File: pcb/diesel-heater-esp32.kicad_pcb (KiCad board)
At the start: 2 copper layers, 60 x 45 mm, 29 parts, among them J1 5V Power, J10 Fan Motor, J11 Glow Plug, J12 Oil Pump, J2 ESP32 Left, J3 Hall Sensor, J4 Buttons, J5 Battery Mon, J6 ESP32 Right, J7 OLED, J8 NTC50K Room Temperatire, J9 NTC50K Outlet Temperatire

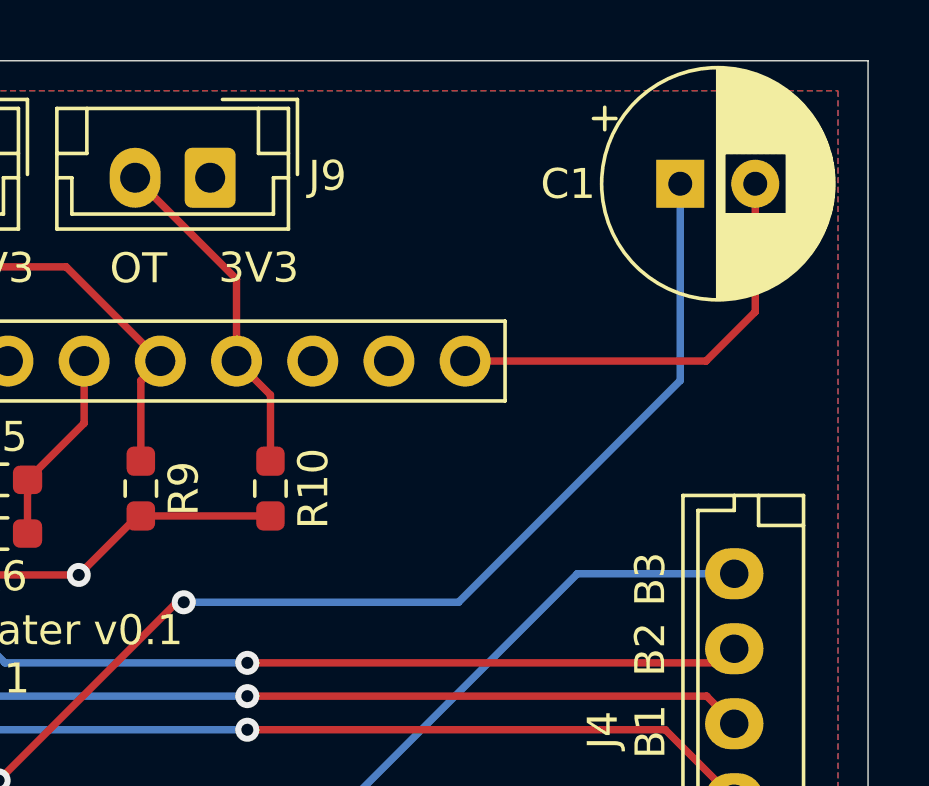
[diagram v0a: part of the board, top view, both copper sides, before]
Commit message: capacitor value fixed. capacitor sized set to 6.3mm
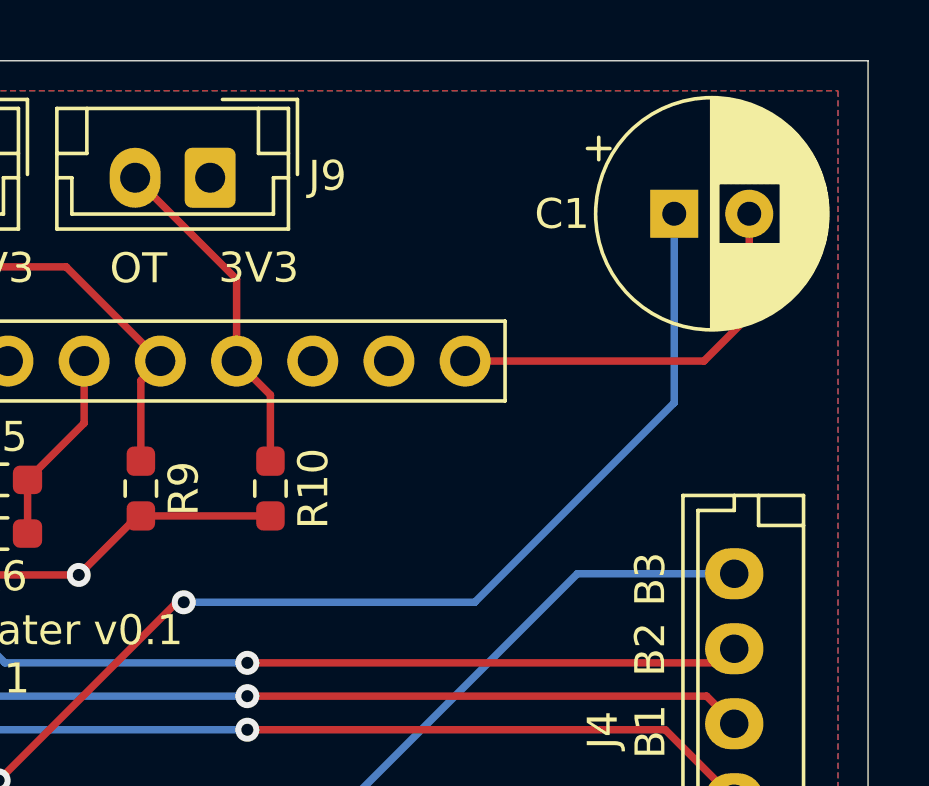
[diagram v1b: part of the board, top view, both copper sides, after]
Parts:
- C1: value CP1 -> 470uF
- moved C1 1.02 mm to (167.8, 73.0)
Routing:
- net /EN: track 14.6 -> 13.5 mm
- net /5V: track 73.1 -> 72.3 mm

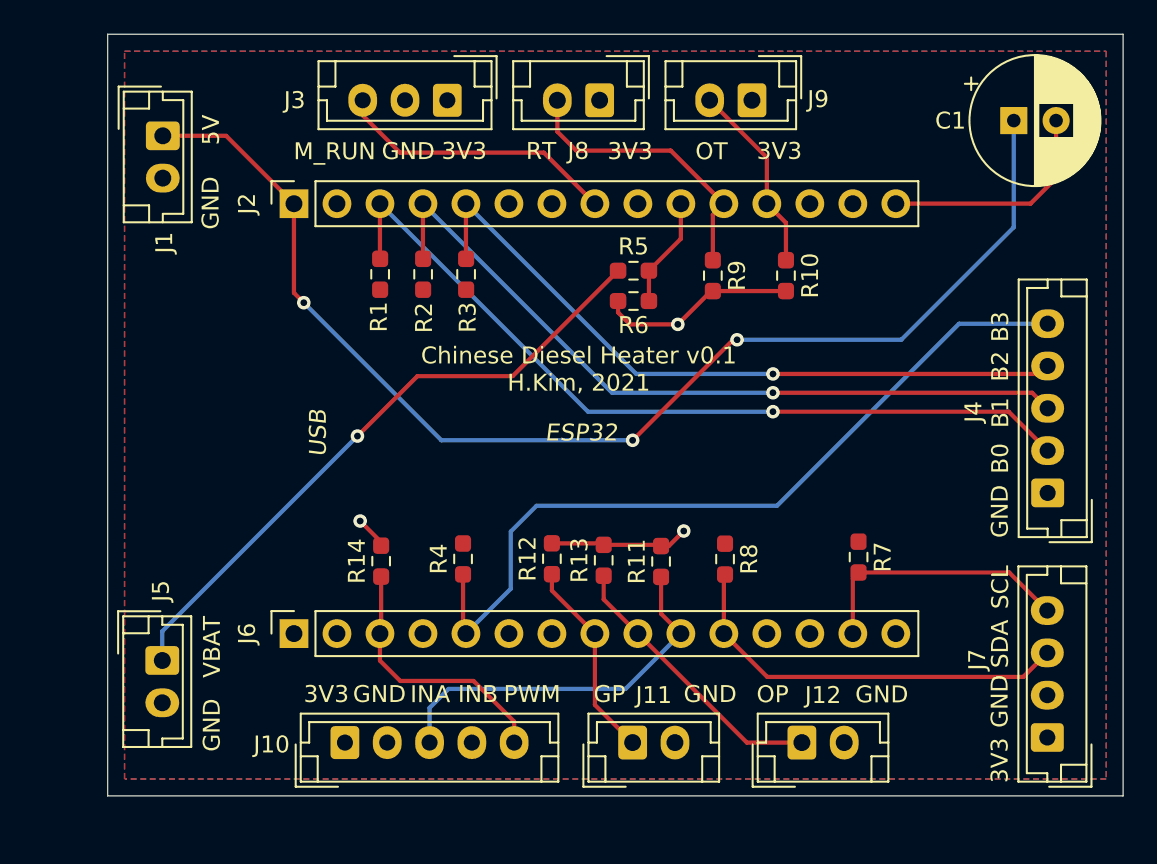
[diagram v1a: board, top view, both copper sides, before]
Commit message: fixed bug in en bug workaround circult. capacitor should be connected to EN and grounded
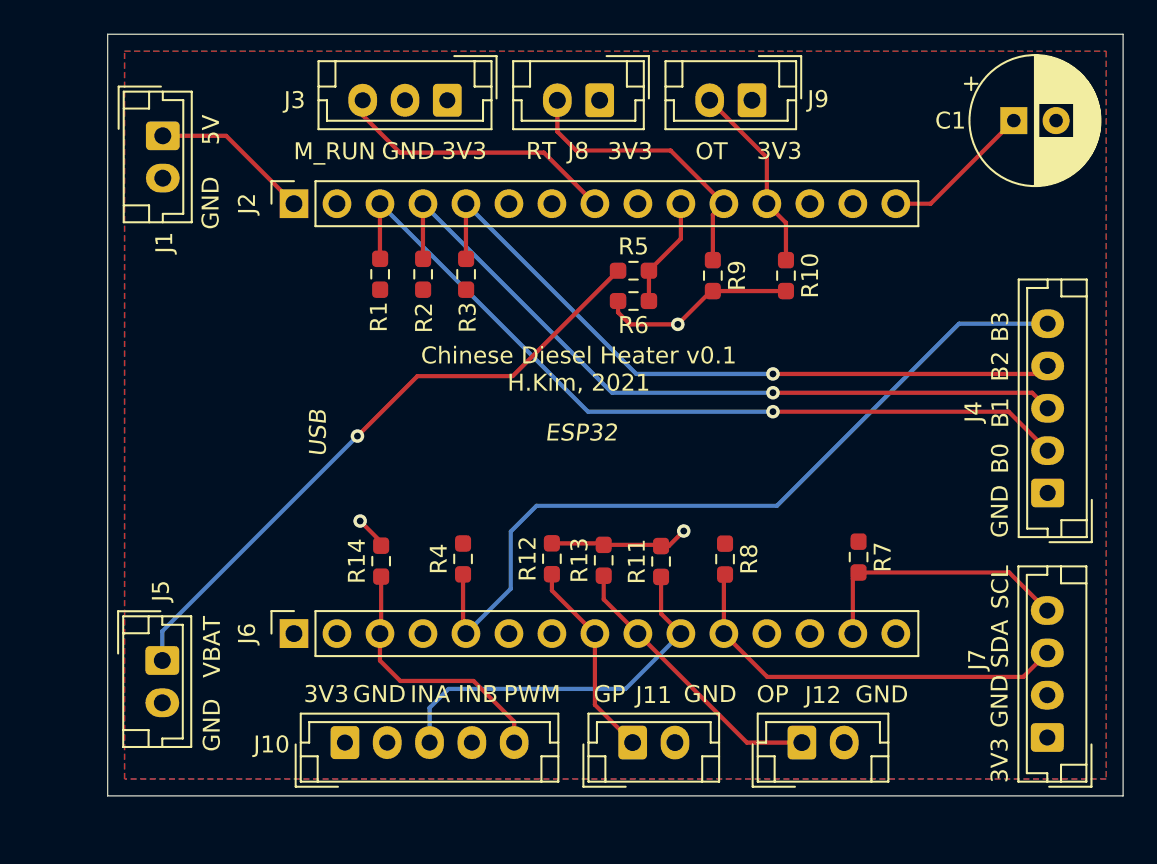
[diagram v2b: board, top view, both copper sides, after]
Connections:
- C1 pad 1: /5V -> /EN
- C1 pad 2: /EN -> GND
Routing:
- net /5V: track 72.3 -> 9.41 mm, vias 3 -> 0
- net /EN: track 13.5 -> 9.00 mm

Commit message: changed pcb layout to fit esp32 dimension
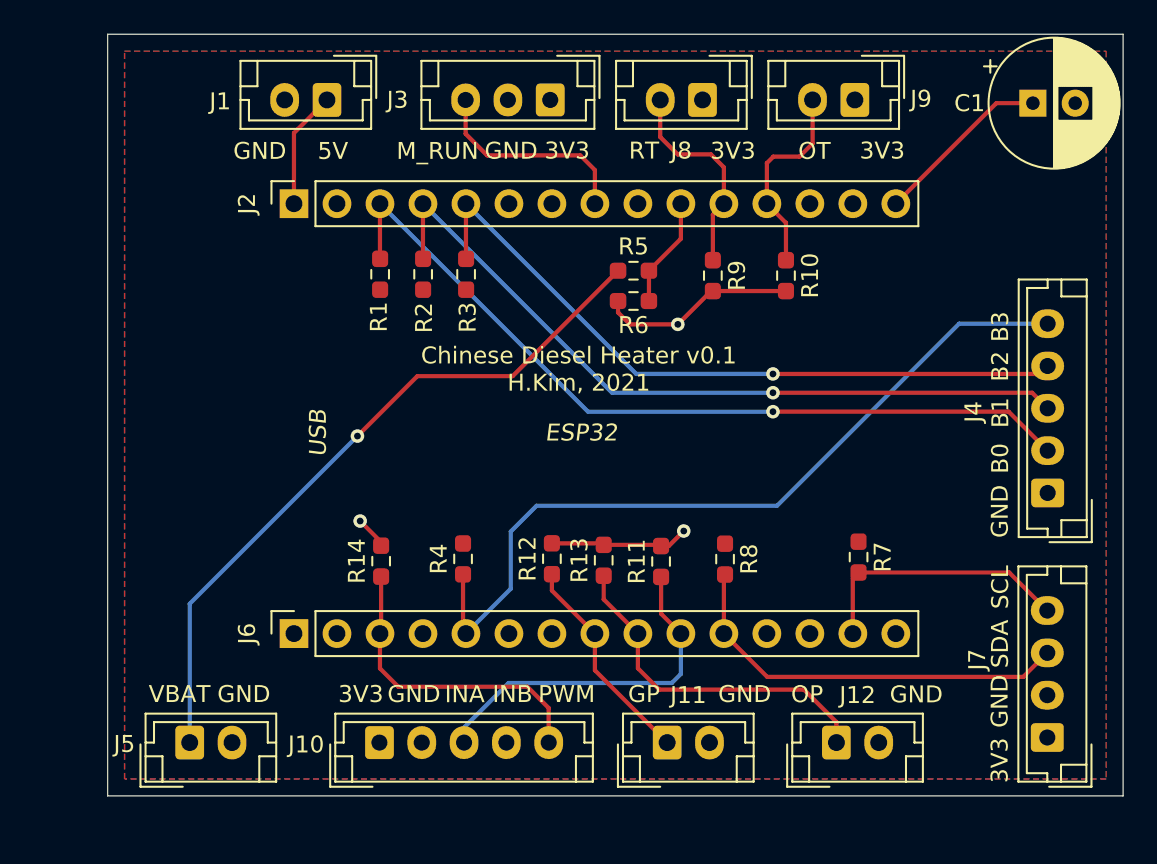
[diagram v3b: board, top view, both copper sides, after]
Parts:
- moved J1 9.93 mm to (127.2, 71.8), turned to 180 degrees
- moved J3 6.08 mm to (140.4, 71.8)
- moved J8 6.08 mm to (149.4, 71.8)
- moved J9 6.08 mm to (158.4, 71.8)
- moved J5 5.11 mm to (119.1, 109.8), turned to 0 degrees
- moved J10 2.04 mm to (130.3, 109.8)
- moved J11 2.04 mm to (147.3, 109.8)
- moved J12 2.04 mm to (157.3, 109.8)
- moved C1 1.53 mm to (168.9, 72.0)
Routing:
- net /RT: track 17.1 -> 12.4 mm
- net /M_RUN: track 16.8 -> 12.5 mm
- net /VBAT: track 37.5 -> 41.7 mm
- net /OP_SIG: track 16.6 -> 20.6 mm
- net /M_PWM: track 15.7 -> 18.4 mm
- net /5V: track 9.41 -> 6.94 mm
- net /EN: track 9.00 -> 10.6 mm
- net /M_INA: track 22.6 -> 21.2 mm
- net /GP_SIG: track 11.9 -> 12.8 mm
- net /OT: track 11.3 -> 12.0 mm

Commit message: releasing pcb 0.1
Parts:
- moved C1 4.65 mm to (164.7, 74.0)
- moved J4 4.65 mm to (165.6, 97.0)
- moved R1 4.65 mm to (126.2, 84.1)
- moved R10 4.65 mm to (150.1, 84.2)
- moved R11 4.65 mm to (142.8, 101.0)
- moved R2 4.65 mm to (128.7, 84.1)
- moved R5 4.65 mm to (141.1, 83.9)
- moved R6 4.65 mm to (141.1, 85.7)
- moved R8 4.65 mm to (146.5, 100.9)
- moved R9 4.65 mm to (145.8, 84.2)
- moved J1 4.65 mm to (123.0, 73.8)
- moved J2 4.65 mm to (121.1, 79.9)
- moved J5 4.65 mm to (114.9, 111.8)
- moved J6 4.65 mm to (121.1, 105.3)
- moved REF** 4.65 mm to (119.3, 91.0)
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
